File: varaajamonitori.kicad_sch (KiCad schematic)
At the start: 76 parts, among them J1 230Vin, J11 Conn_01x02_Socket, J3 AVR-ISP-6, J4 sensorAAB, J5 SensorBCC, J6 RO1-230VAC-PUMP, J7 RO2-230VAC-PUMP, Q1 BC337, Q2 BC337, Q3 BT136-500, Q4 BT136-500, Q5 NPN, SW1 UpSw, SW2 DwnSw, SW3 RightSw, SW4 LeftSw, SW5 SelSw, SW6 RetSw, SW7 Reset, SW8 Test1, SW9 Test2, T1 FS12-090-C2, U1 ATmega168-20AU, U3 L7805CV, U6 MOC3020M, U7 MOC3020M

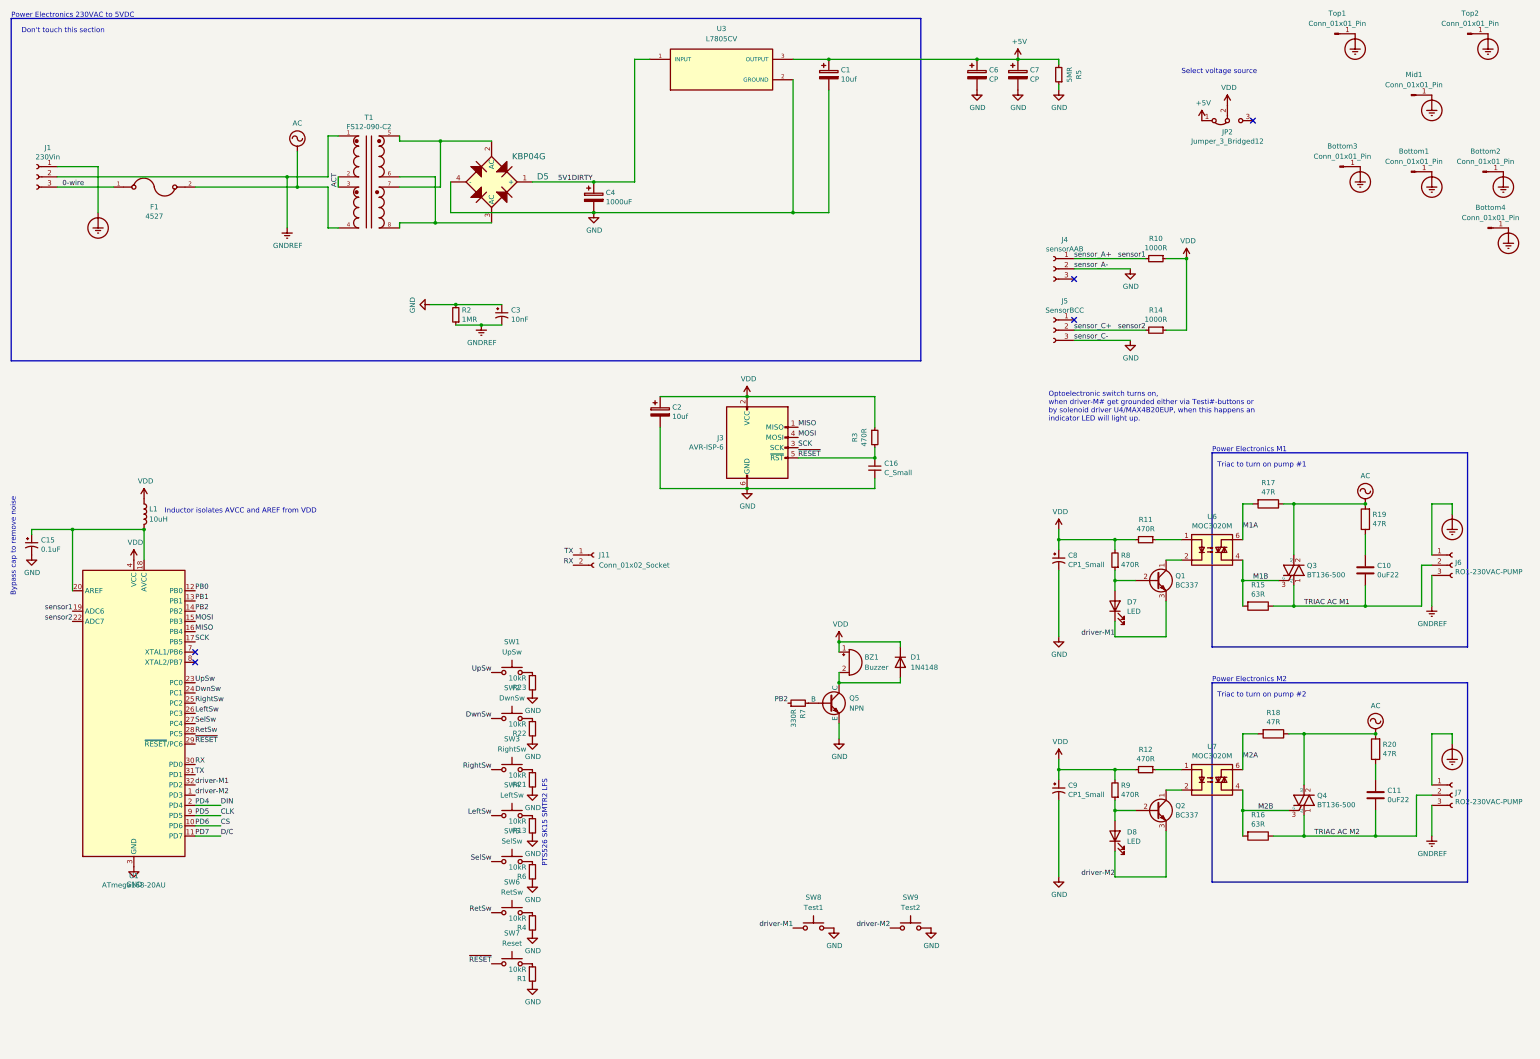
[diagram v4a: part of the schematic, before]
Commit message: Adding ISP, UART, I2C plus commenting
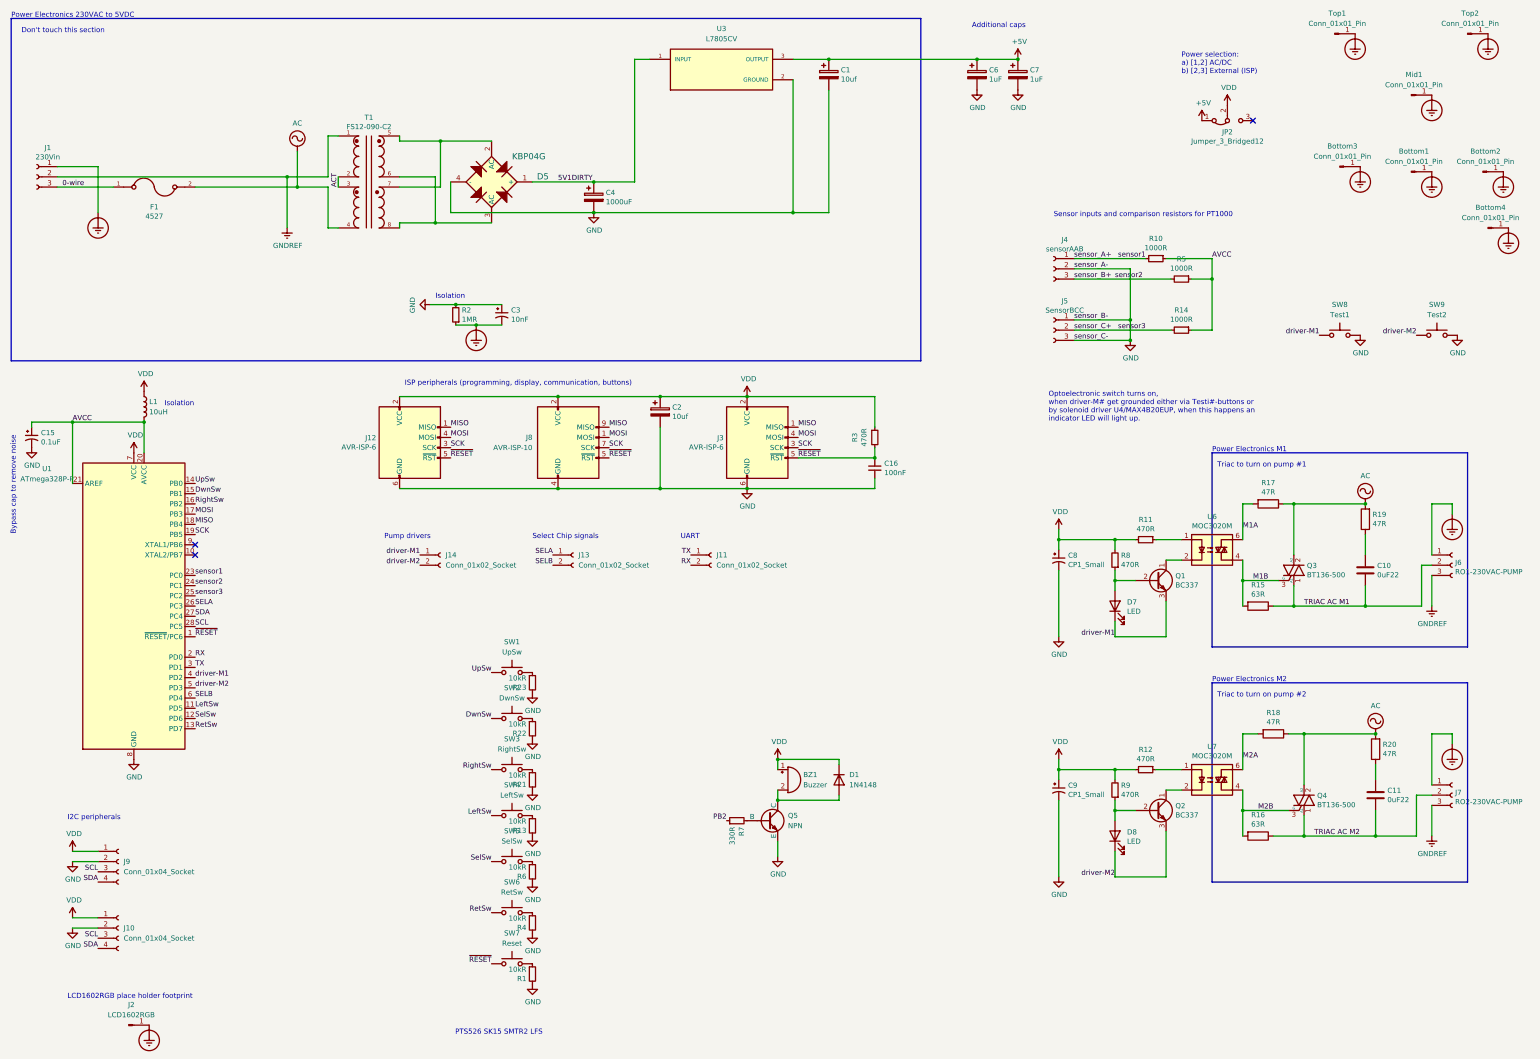
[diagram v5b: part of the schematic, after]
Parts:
- removed U1: ATmega168-20AU, Package_QFP:TQFP-32_7x7mm_P0.8mm, symbol varaajamonitori-rescue:ATmega168-20AU-MCU_Microchip_ATmega
- added J10, J9: Conn_01x04_Socket, Connector_PinHeader_2.54mm:PinHeader_1x04_P2.54mm_Vertical, symbol Connector:Conn_01x04_Socket
- added J12: AVR-ISP-6, Connector_PinHeader_2.54mm:PinHeader_2x03_P2.54mm_Vertical, symbol Connector:AVR-ISP-6
- added J13, J14: Conn_01x02_Socket, Connector_PinHeader_2.54mm:PinHeader_1x02_P2.54mm_Vertical, symbol Connector:Conn_01x02_Socket
- added J2: LCD1602RGB, varaajamonitori:LCD1602 RGB MOD, symbol Connector:Conn_01x01_Pin
- added J8: AVR-ISP-10, Connector_PinHeader_2.54mm:PinHeader_2x05_P2.54mm_Vertical, symbol Connector:AVR-ISP-10
- added U1: ATmega328P-P, Package_DIP:DIP-28_W7.62mm, symbol MCU_Microchip_ATmega:ATmega328P-P
- C15, C3, C8, C9: footprint Capacitor_THT:CP_Radial_Tantal_D4.5mm_P5.00mm -> Capacitor_SMD:C_1206_3216Metric_Pad1.33x1.80mm_HandSolder
- C16: value C_Small -> 100nF; footprint Capacitor_THT:C_Disc_D3.0mm_W1.6mm_P2.50mm -> Capacitor_SMD:C_1206_3216Metric_Pad1.33x1.80mm_HandSolder
- C6, C7: value CP -> 1uF
- L1: footprint Inductor_THT:L_Axial_L5.3mm_D2.2mm_P2.54mm_Vertical_Vishay_IM-1 -> Inductor_SMD:L_1206_3216Metric_Pad1.22x1.90mm_HandSolder
- R1: footprint Resistor_THT:R_Axial_DIN0309_L9.0mm_D3.2mm_P12.70mm_Horizontal -> Resistor_SMD:R_1206_3216Metric_Pad1.30x1.75mm_HandSolder
- R11, R12, R3, R8, R9: footprint Resistor_SMD:R_0805_2012Metric_Pad1.20x1.40mm_HandSolder -> Resistor_SMD:R_1206_3216Metric_Pad1.30x1.75mm_HandSolder
- R13, R21, R22, R23, R4, R6, R7: footprint Resistor_THT:R_Axial_DIN0309_L9.0mm_D3.2mm_P12.70mm_Horizontal -> Resistor_SMD:R_0805_2012Metric_Pad1.20x1.40mm_HandSolder
- R5: value 5MR -> 1000R; footprint Resistor_SMD:R_1206_3216Metric_Pad1.30x1.75mm_HandSolder -> Resistor_SMD:R_0805_2012Metric_Pad1.20x1.40mm_HandSolder
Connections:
- net +5V: no longer R5.2
- net DwnSw: now also U1.15 (PB1)
- net Earth_Protective: now also C3.2, R2.1, J2.1 (Pin_1)
- net GND: now also J5.1 (Pin_1), J10.2 (Pin_2), J12.6 (GND), J8.10 (GND), J8.4 (GND), J8.6 (GND), J8.8 (GND), J9.2 (Pin_2), U1.22 (GND), U1.8 (GND); no longer R5.1
- net GNDREF: no longer C3.2, R2.1
- net LeftSw: now also U1.11 (PD5)
- net MISO: now also J12.1 (MISO), J8.9 (MISO), U1.18 (PB4)
- net MOSI: now also J12.4 (MOSI), J8.1 (MOSI), U1.17 (PB3)
- net RX: now also U1.2 (PD0)
- net RetSw: now also U1.13 (PD7)
- net RightSw: now also U1.16 (PB2)
- net SCK: now also J12.3 (SCK), J8.7 (SCK), U1.19 (PB5)
- net SelSw: now also U1.12 (PD6)
- net TX: now also U1.3 (PD1)
- net UpSw: now also U1.14 (PB0)
- net VDD: now also J10.1 (Pin_1), J12.2 (VCC), J8.2 (VCC), J9.1 (Pin_1), U1.7 (VCC); no longer R10.1, R14.1
- net driver-M1: now also J14.1 (Pin_1), U1.4 (PD2)
- net driver-M2: now also J14.2 (Pin_2), U1.5 (PD3)
- net sensor1: now also U1.23 (PC0)
- net sensor2: now also J4.3 (Pin_3), R5.2, U1.24 (PC1); no longer J5.2 (Pin_2), R14.2
- net ~{RESET}: now also J12.5 (~{RST}), J8.5 (~{RST}), U1.1 (~{RESET}/PC6)
- net AVCC: now reaches C15.1, L1.2
- net AVCC: now also R10.1, R14.1, R5.1, U1.20 (AVCC), U1.21 (AREF)
- new net SCL: J10.3 (Pin_3), J9.3 (Pin_3), U1.28 (PC5)
- new net SDA: J10.4 (Pin_4), J9.4 (Pin_4), U1.27 (PC4)
- new net SELA: J13.1 (Pin_1), U1.26 (PC3)
- new net SELB: J13.2 (Pin_2), U1.6 (PD4)
- new net sensor3: J5.2 (Pin_2), R14.2, U1.25 (PC2)
- no-connect marks 5 -> 3
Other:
- note added: "Additional caps"
- note added: "I2C peripherals"
- note added: "ISP peripherals (programming, display, communication, buttons)"
- note added: "Isolation"
- note added: "LCD1602RGB place holder footprint"
- note added: "Power selection: a) [1,2] AC/DC b) [2,3] External (ISP)"
- note added: "Pump drivers"
- note added: "Select Chip signals"
- note added: "Sensor inputs and comparison resistors for PT1000"
- note added: "UART"
- note removed: "Inductor isolates AVCC and AREF from VDD"
- note removed: "Select voltage source"
- moved on the sheet: BZ1, C15, D1, J11, L1, Q5, R14, R7, SW8, SW9

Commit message: some changes
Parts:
- removed C1: 10uf, Capacitor_THT:CP_Radial_D6.3mm_P2.50mm, symbol varaajamonitori-rescue:CP-Device
- removed C10, C11: 0uF22, Capacitor_THT:C_Rect_L18.0mm_W9.0mm_P15.00mm_FKS3_FKP3, symbol Device:C
- removed C15: 0.1uF, Capacitor_SMD:C_1206_3216Metric_Pad1.33x1.80mm_HandSolder, symbol varaajamonitori-rescue:CP1_Small-Device
- removed C3: 10nF, Capacitor_SMD:C_1206_3216Metric_Pad1.33x1.80mm_HandSolder, symbol varaajamonitori-rescue:CP1_Small-Device
- removed C4: 1000uF, Capacitor_THT:CP_Radial_D8.0mm_P3.50mm, symbol varaajamonitori-rescue:CP-Device
- removed C6, C7: 1uF, Capacitor_THT:CP_Radial_D6.3mm_P2.50mm, symbol varaajamonitori-rescue:CP-Device
- removed C8, C9: CP1_Small, Capacitor_SMD:C_1206_3216Metric_Pad1.33x1.80mm_HandSolder, symbol varaajamonitori-rescue:CP1_Small-Device
- removed D5: KBP04G, digikey-footprints:SIP-4_W3.81mm, symbol varaajamonitori-rescue:KBP04G-dk_Diodes-Bridge-Rectifiers
- removed D7, D8: LED, LED_THT:LED_D3.0mm, symbol Device:LED
- removed F1: 4527, FUSE_4527, symbol varaajamonitori-rescue:4527-4527
- removed J1: 230Vin, varaajamonitori:side3poscon, symbol Connector:Conn_01x03_Female
- removed J12: AVR-ISP-6, Connector_PinHeader_2.54mm:PinHeader_2x03_P2.54mm_Vertical, symbol Connector:AVR-ISP-6
- removed J13: Conn_01x02_Socket, Connector_PinHeader_2.54mm:PinHeader_1x02_P2.54mm_Vertical, symbol Connector:Conn_01x02_Socket
- removed J6: RO1-230VAC-PUMP, varaajamonitori:side3poscon, symbol Connector:Conn_01x03_Female
- removed J7: RO2-230VAC-PUMP, varaajamonitori:side3poscon, symbol Connector:Conn_01x03_Female
- removed Q1, Q2: BC337, Package_TO_SOT_THT:TO-92_Inline, symbol Transistor_BJT:BC337
- removed Q3, Q4: BT136-500, Package_TO_SOT_THT:TO-220-3_Vertical, symbol Triac_Thyristor:BT136-500
- removed Q5: NPN, Package_TO_SOT_THT:TO-92_Inline, symbol Simulation_SPICE:NPN
- removed R11, R8, R9: 470R, Resistor_SMD:R_1206_3216Metric_Pad1.30x1.75mm_HandSolder, symbol Device:R_Small
- removed R15, R16: 63R, Resistor_THT:R_Axial_DIN0414_L11.9mm_D4.5mm_P15.24mm_Horizontal, symbol Device:R
- removed R17, R18, R19, R20: 47R, Resistor_THT:R_Axial_DIN0414_L11.9mm_D4.5mm_P15.24mm_Horizontal, symbol Device:R
- removed R2: 1MR, Resistor_SMD:R_0805_2012Metric_Pad1.20x1.40mm_HandSolder, symbol Device:R_Small
- removed R7: 330R, Resistor_SMD:R_0805_2012Metric_Pad1.20x1.40mm_HandSolder, symbol Device:R_Small
- removed SW8: Test1, Button_Switch_SMD:SW_Push_1P1T_NO_CK_KSC6xxJ, symbol Switch:SW_Push
- removed SW9: Test2, Button_Switch_SMD:SW_Push_1P1T_NO_CK_KSC6xxJ, symbol Switch:SW_Push
- removed T1: FS12-090-C2, XFMR_FS12-090-C2, symbol FS12-090-C2:FS12-090-C2
- removed U3: L7805CV, varaajamonitori2:TO255P1040X460X1968-3, symbol L7805CV:L7805CV
- removed U6, U7: MOC3020M, Package_DIP:DIP-6_W7.62mm_LongPads, symbol Relay_SolidState:MOC3020M
- added C13: 100nF, Capacitor_SMD:C_1206_3216Metric_Pad1.33x1.80mm_HandSolder, symbol Device:C_Small
- added D2, D4: LED, LED_THT:LED_D3.0mm, symbol Device:LED
- added D3: 1N4148W-TP, Diode_SMD:D_SOD-123, symbol Device:D
- added J12: AVR-ISP-10, Connector_PinHeader_2.54mm:PinHeader_2x05_P2.54mm_Vertical, symbol Connector:AVR-ISP-10
- added R24: 390R, Resistor_SMD:R_1206_3216Metric_Pad1.30x1.75mm_HandSolder, symbol Device:R_Small
- BZ1: footprint Buzzer_Beeper:Buzzer_12x9.5RM7.6 -> footprints:CEM-1206S_CUD; Digi-Key_PN (none) -> 102-1155-ND
- C16: value 100nF -> 1uF
- C2: value 10uf -> 10uF
- D1: value 1N4148 -> 1N4148W-TP; footprint Diode_THT:D_DO-35_SOD27_P7.62mm_Horizontal -> Diode_SMD:D_SOD-123; Digi-Key_PN (none) -> 1N4148WTPMSCT-ND
- J3: Digi-Key_PN (none) -> 732-5394-ND
- J4: value sensorAAB -> SensorAAB
- J8: Digi-Key_PN (none) -> ED1543-ND
- R1: Digi-Key_PN (none) -> 541-10.0KFTR-ND
- R10, R14, R5: footprint Resistor_SMD:R_0805_2012Metric_Pad1.20x1.40mm_HandSolder -> Resistor_SMD:R_1206_3216Metric_Pad1.30x1.75mm_HandSolder; Digi-Key_PN (none) -> 749-1055-2-ND
- R12: value 470R -> 390R; Digi-Key_PN (none) -> 541-390FTR-ND
- R13, R21, R22, R23, R4, R6: footprint Resistor_SMD:R_0805_2012Metric_Pad1.20x1.40mm_HandSolder -> Resistor_SMD:R_1206_3216Metric_Pad1.30x1.75mm_HandSolder; Digi-Key_PN (none) -> 541-10.0KFTR-ND
- R3: Digi-Key_PN (none) -> 541-470FTR-ND
- SW1, SW2, SW3, SW4, SW5, SW6, SW7: footprint Button_Switch_SMD:SW_Push_1P1T_NO_CK_KSC6xxJ -> Button_Switch_SMD:SW_Push_1P1T_NO_6x6mm_H9.5mm; Digi-Key_PN (none) -> EG1868TR-ND
- U1: Digi-Key_PN (none) -> 952-2748-ND
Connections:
- net SELB is gone; now on net ~{BUZZ}: U1.6 (PD4)
- net AVCC: now also C13.1
- net GND: now also C13.2, J12.10 (GND), J12.4 (GND), J12.6 (GND), J12.8 (GND)
- net MISO: now also J12.9 (MISO)
- net MOSI: now also J12.1 (MOSI)
- net RX: now also D4.1 (K)
- net SCK: now also J12.7 (SCK)
- net SELA: now also J8.3 (CH), J12.3 (CH)
- net TX: now also D2.1 (K)
- net VDD: now also D3.1 (K), J12.2 (VCC), R24.2
- net ~{RESET}: now also D3.2 (A), J12.5 (~{RST})
- net at R12.1: now also D2.2 (A)
- net ~{BUZZ}: now reaches BZ1.2 (+), D1.2 (A)
- new net: D4.2 (A), R24.1
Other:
- added sheet AC230DC5 (trans.kicad_sch)
- added sheet TRIAC (triac.kicad_sch)
- note added: "ISP peripherals (programming, display, communication, buttons) ISP6 is dedicated to AVR programming while ~{RESET} ISP10 J8 and J12, has chip select feature"
- note added: "Indicators"
- note added: "Power selection for testing a) [1,2] AC/DC b) [2,3] AC disconnected"
- note added: "Pump driver test pins"
- note added: "Screw holes with earth shielding"
- note added: "Start-up delay"
- note removed: "Additional caps"
- note removed: "Don't touch this section"
- note removed: "ISP peripherals (programming, display, communication, buttons)"
- note removed: "Optoelectronic switch turns on, when driver-M# get grounded either via Testi#-buttons or by solenoid driver U4/MAX4B20EUP, when this happens an indicator LED will light up."
- note removed: "PTS526 SK15 SMTR2 LFS"
- note removed: "Power Electronics 230VAC to 5VDC"
- note removed: "Power Electronics M1"
- note removed: "Power Electronics M2"
- note removed: "Power selection: a) [1,2] AC/DC b) [2,3] External (ISP)"
- note removed: "Pump drivers"
- note removed: "Select Chip signals"
- note removed: "Triac to turn on pump #1"
- note removed: "Triac to turn on pump #2"
- moved on the sheet: BZ1, Bottom1, Bottom2, Bottom3, Bottom4, C16, C2, D1, J10, J11, J14, J2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
